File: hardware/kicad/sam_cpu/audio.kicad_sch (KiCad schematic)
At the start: 56 parts, among them J10 J10 SPEAKERS, J22 J22 STEREO, J24 J24 SUBWOOFER, Q4 2N7002, U22 PCM5102A, U23 TDA7297, U24 TDA7297, U26 OPA1678

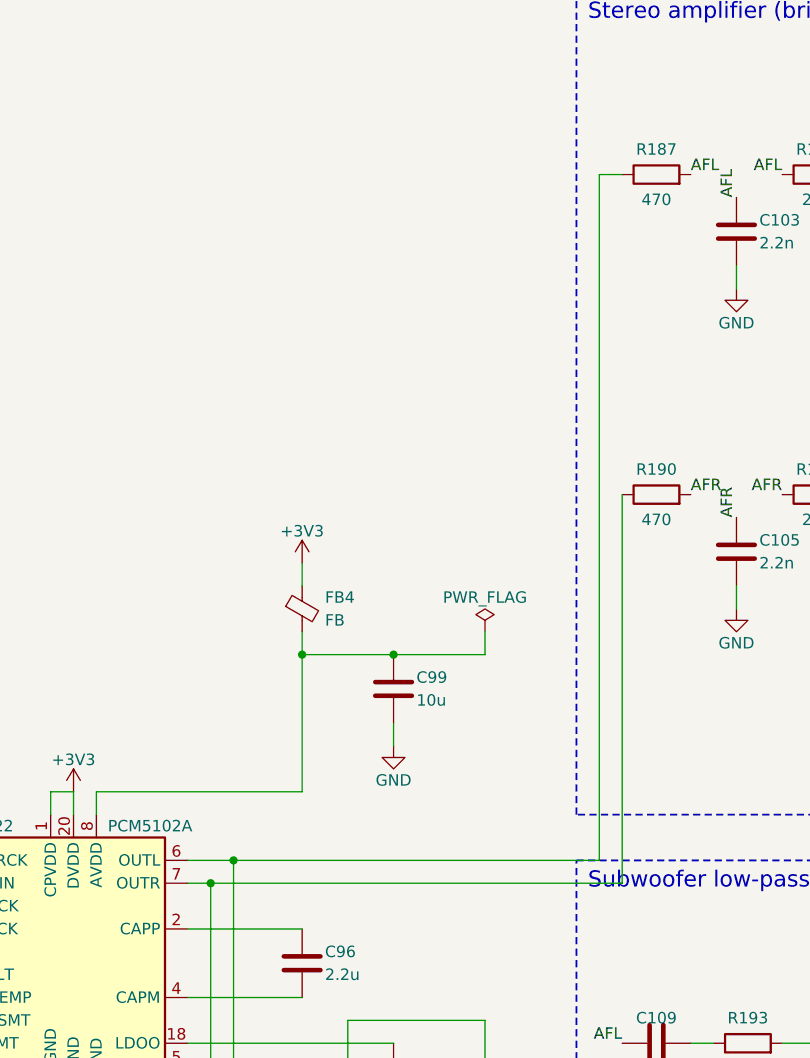
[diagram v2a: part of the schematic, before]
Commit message: Isolated RS485 (ADM2682E, two top-entry RJ45s), line-in jack, board extension back, MH3 lowered
- Page 13: ADM2682E with the cable side on GND_ISO, J27 in / J29 out (OST PJ012
  vertical), J30 switched 3.5 mm line-in between the DAC and the amplifiers.
- Audio sheet: DAC output wires split into AUD_DAC_L/R and AUD_AMP_L/R for J30.
- Board: 142 mm extension below the Pi restored, GND_ISO zone with a 2 mm gap,
  MH3 screw position moved down 7.42 mm (open notch), page-13 parts re-placed.
- Change scripts c16-c18; ERC 0, DRC schematic parity 0.

Co-Authored-By: Claude Opus 5.5 (1M context) <noreply@anthropic.com>
Claude-Session: https://claude.ai/code/session_01ExuDVoDDDHhVWjb8EwVzYb
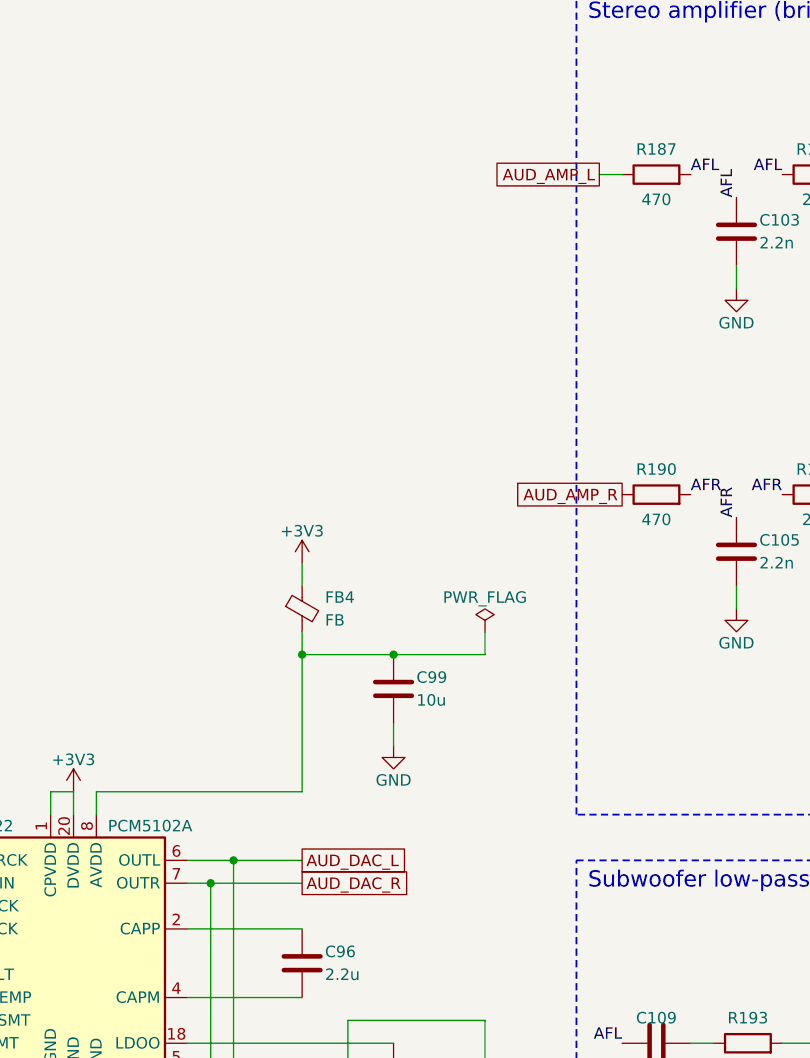
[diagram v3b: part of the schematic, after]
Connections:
- net AUD_DAC_L: now reaches TP19.1, U22.6 (OUTL)
- net AUD_DAC_L: no longer R187.1
- net AUD_DAC_R: now reaches TP20.1, U22.7 (OUTR)
- net AUD_DAC_R: no longer R190.1
- new net AUD_AMP_L: R187.1
- new net AUD_AMP_R: R190.1
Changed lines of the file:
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@@
-	(wire
-		(pts
-			(xy 137.16 134.62) (xy 137.16 91.44)
-		)
-		(stroke
-			(width 0)
-			(type default)
-		)
-	)
 	(wire
 		(pts
@@
 	(wire
 		(pts
+			(xy 88.9 132.08) (xy 101.6 132.08)
+		)
+		(stroke
+			(width 0)
+			(type default)
+		)
+	)
+	(wire
+		(pts
+			(xy 88.9 134.62) (xy 101.6 134.62)
+		)
+		(stroke
+			(width 0)
+			(type default)
+		)
+	)
+	(wire
+		(pts
 			(xy 287.02 228.6) (xy 289.56 228.6)
 		)
@@
 	(wire
 		(pts
-			(xy 88.9 132.08) (xy 134.62 132.08)
-		)
-		(stroke
-			(width 0)
-			(type default)
-		)
-	)
-	(wire
-		(pts
 			(xy 91.44 218.44) (xy 55.88 218.44)
 		)
@@
 	(wire
 		(pts
-			(xy 134.62 132.08) (xy 134.62 55.88)
-		)
-		(stroke
-			(width 0)
-			(type default)
-		)
-	)
-	(wire
-		(pts
 			(xy 25.4 185.42) (xy 25.4 187.96)
-		)
-		(stroke
-			(width 0)
-			(type default)
-		)
-	)
-	(wire
-		(pts
-			(xy 88.9 134.62) (xy 137.16 134.62)
 		)
 		(stroke
@@
 		)
 	)
+	(global_label "AUD_AMP_R"
+		(shape passive)
+		(at 137.16 91.44 180)
+		(fields_autoplaced yes)
+		(effects
+			(font
+				(size 1.27 1.27)
+			)
+			(justify right)
+		)
+		(property "Intersheetrefs" "${INTERSHEET_REFS}"
+			(at 122.41 91.44 180)
+			(show_name no)
+			(do_not_autoplace no)
+			(effects
+				(font
+					(size 1.27 1.27)
+				)
+				(justify right)
+			)
+		)
+	)
+	(global_label "AUD_DAC_R"
+		(shape passive)
+		(at 101.6 134.62 0)
+		(fields_autoplaced yes)
+		(effects
+			(font
+				(size 1.27 1.27)
+			)
+			(justify left)
+		)
+		(property "Intersheetrefs" "${INTERSHEET_REFS}"
+			(at 116.35 134.62 0)
+			(show_name no)
+			(do_not_autoplace no)
+			(effects
+				(font
+					(size 1.27 1.27)
+				)
+				(justify left)
+			)
+		)
+	)
 	(global_label "I2S_LRCK"
 		(shape input)
@@
 			)
 		)
+	)
+	(global_label "AUD_AMP_L"
+		(shape passive)
+		(at 134.62 55.88 180)
+		(fields_autoplaced yes)
+		(effects
+			(font
+				(size 1.27 1.27)
+			)
+			(justify right)
+		)
+		(property "Intersheetrefs" "${INTERSHEET_REFS}"
+			(at 119.87 55.88 180)
+			(show_name no)
+			(do_not_autoplace no)
+			(effects
+				(font
+					(size 1.27 1.27)
+				)
+				(justify right)
+			)
+		)
+	)
+	(global_label "AUD_DAC_L"
+		(shape passive)
+		(at 101.6 132.08 0)
+		(fields_autoplaced yes)
+		(effects
+			(font
+				(size 1.27 1.27)
+			)
+			(justify left)
+		)
+		(property "Intersheetrefs" "${INTERSHEET_REFS}"
+			(at 116.35 132.08 0)
+			(show_name no)
+			(do_not_autoplace no)
+			(effects
+				(font
+					(size 1.27 1.27)
+				)
+				(justify left)
+			)
+		)

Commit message: C108/C118: 35 V 470 uF in 8x10 can (CP_Elec_8x10)
Vincent's choice on the 12 V bulk caps. Footprints swapped in place, +12V feed
under C108 moved down, GND fanout vias redone; DRC unchanged, 36 opens.

Co-Authored-By: Claude Opus 5.5 (1M context) <noreply@anthropic.com>
Claude-Session: https://claude.ai/code/session_01ExuDVoDDDHhVWjb8EwVzYb
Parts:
- C108, C118: footprint Capacitor_SMD:CP_Elec_6.3x7.7 -> Capacitor_SMD:CP_Elec_8x10
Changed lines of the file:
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@@
 			)
 		)
-		(property "Footprint" "Capacitor_SMD:CP_Elec_6.3x7.7"
+		(property "Footprint" "Capacitor_SMD:CP_Elec_8x10"
 			(at 277.8252 68.58 0)
 			(hide yes)
@@
 			)
 		)
-		(property "Footprint" "Capacitor_SMD:CP_Elec_6.3x7.7"
+		(property "Footprint" "Capacitor_SMD:CP_Elec_8x10"
 			(at 323.5452 215.9 0)
 			(hide yes)

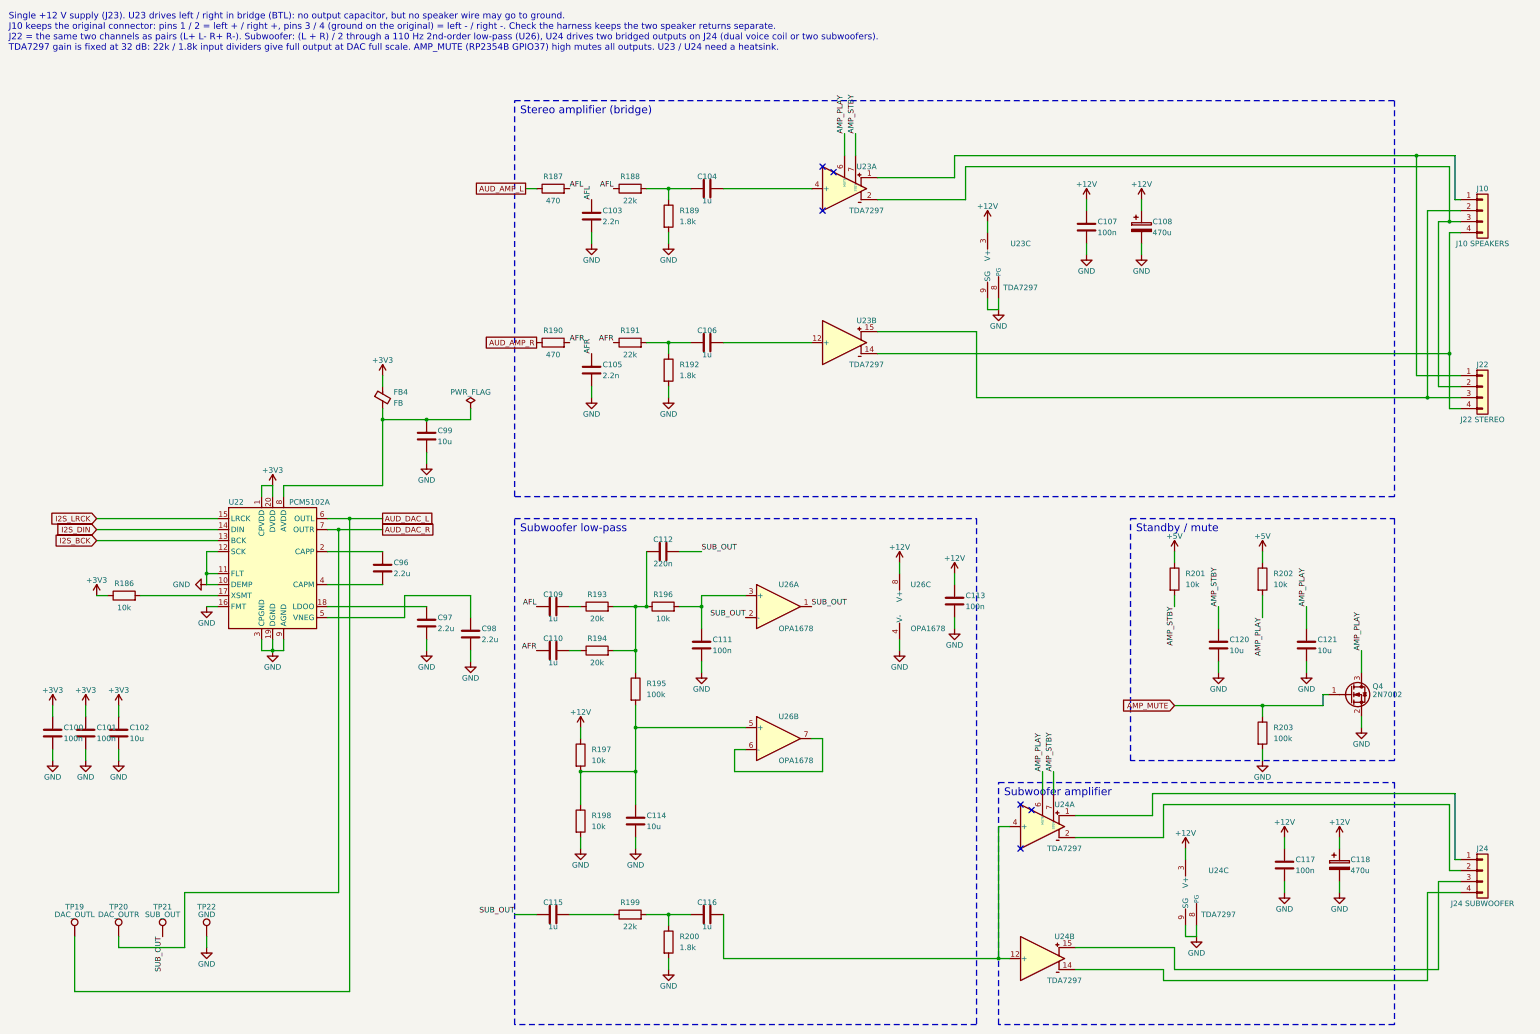
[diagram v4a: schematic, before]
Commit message: DIP switch block not loaded; larger schematic text
c30: SW3, R168-R175, U14 and C93 flagged DNP (schematic and board).
c31: schematic text 1.27 -> 1.6 mm (pins 1.5 mm), intersheet refs moved out.

Co-Authored-By: Claude Opus 5.5 (1M context) <noreply@anthropic.com>
Claude-Session: https://claude.ai/code/session_01ExuDVoDDDHhVWjb8EwVzYb
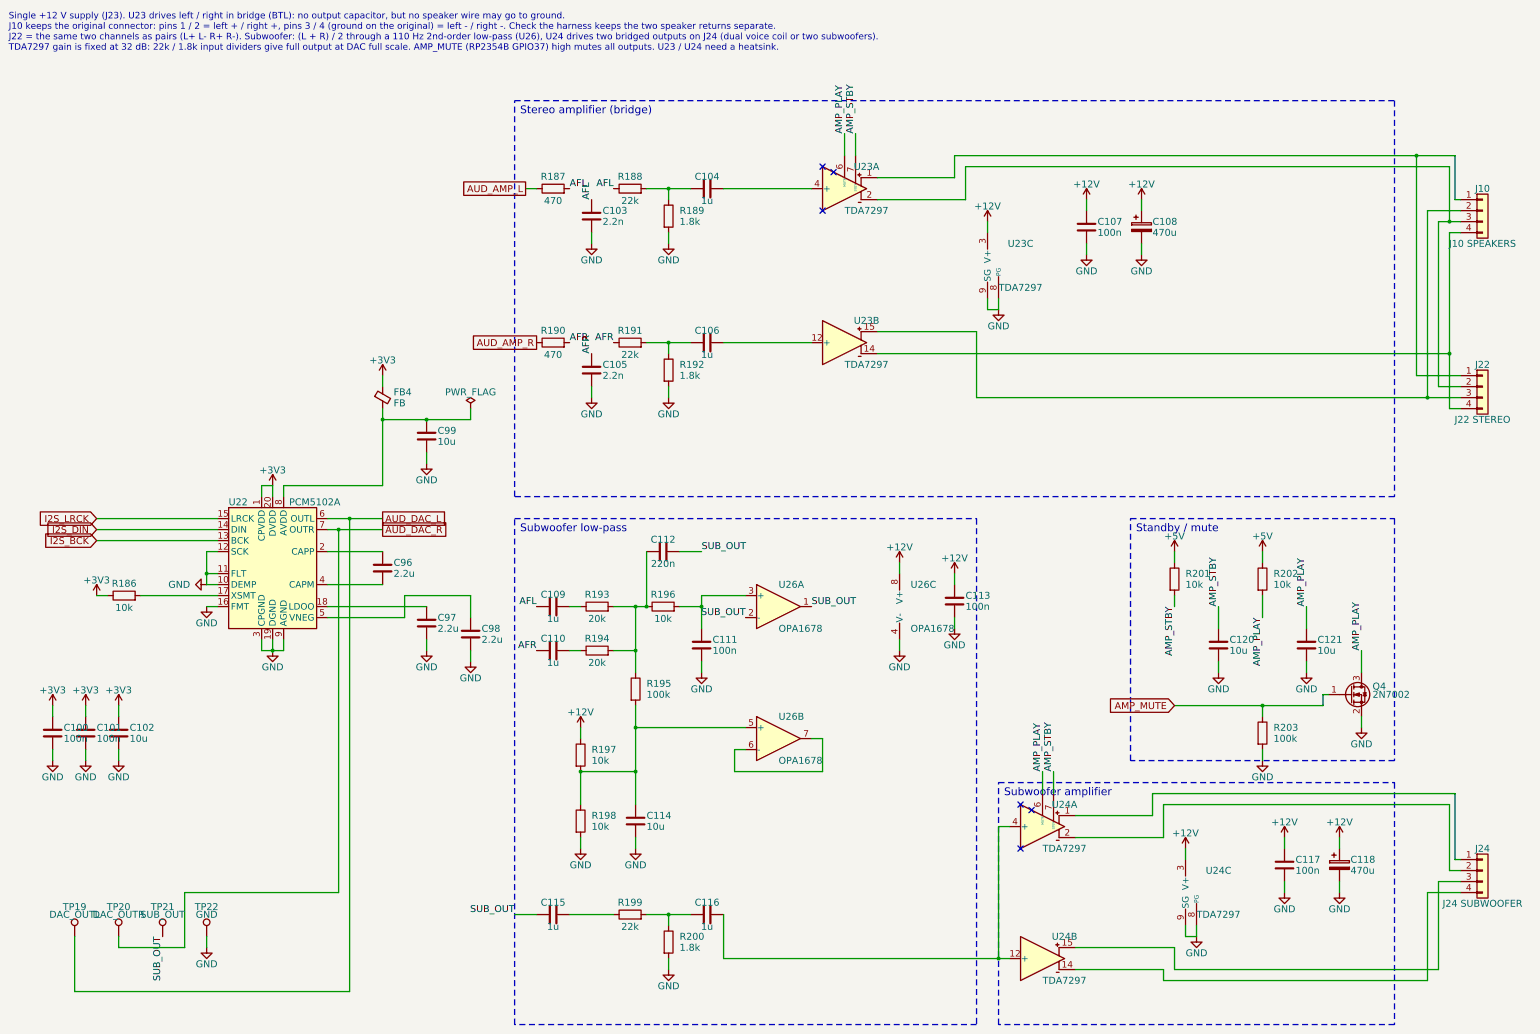
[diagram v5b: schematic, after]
